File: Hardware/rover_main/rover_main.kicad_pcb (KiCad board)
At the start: 2 copper layers, 85 x 70 mm, 36 parts, among them J1 BATT, J10 Analog, J2 BME280, J3 CSS811, J4 DRIVERS, J5 GY-87, J6 PROG, J7 FTDI, J8 Digital, U1 LD1117A33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

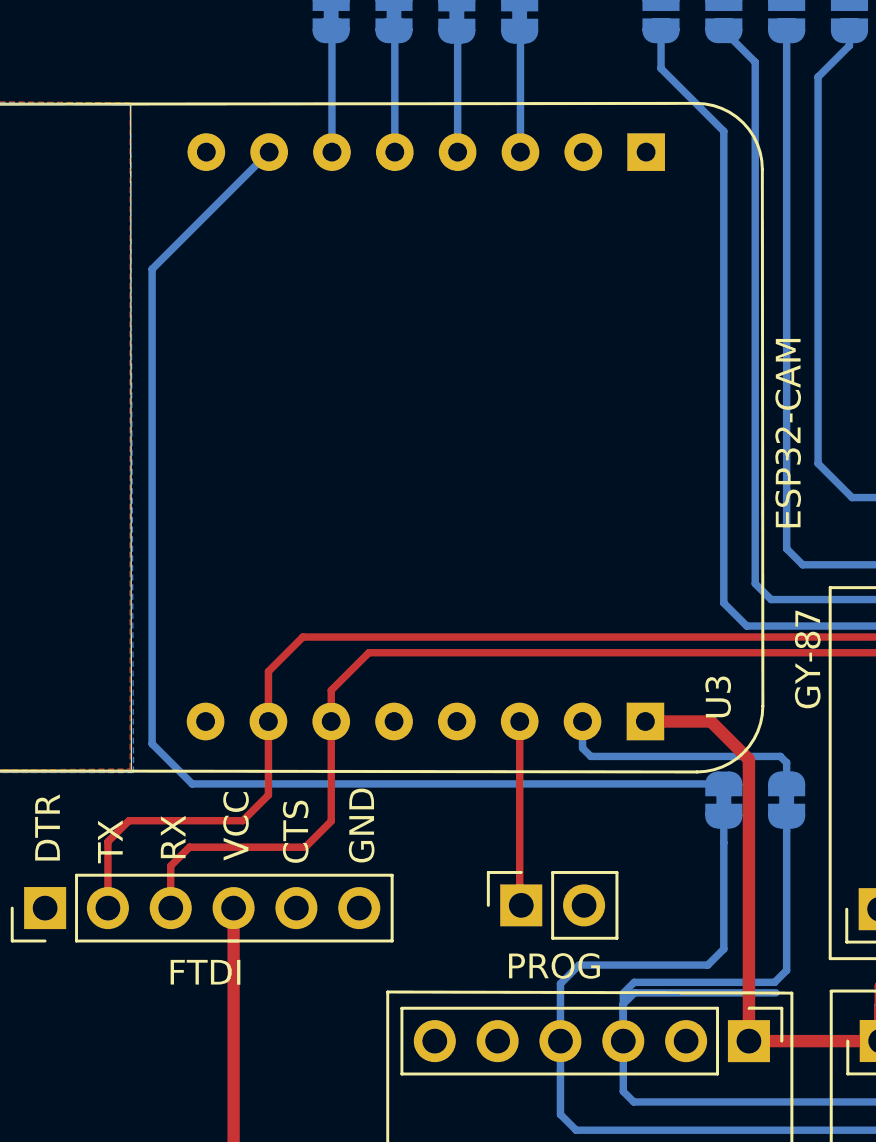
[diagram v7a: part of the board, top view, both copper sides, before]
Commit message: Add SDA to jumper
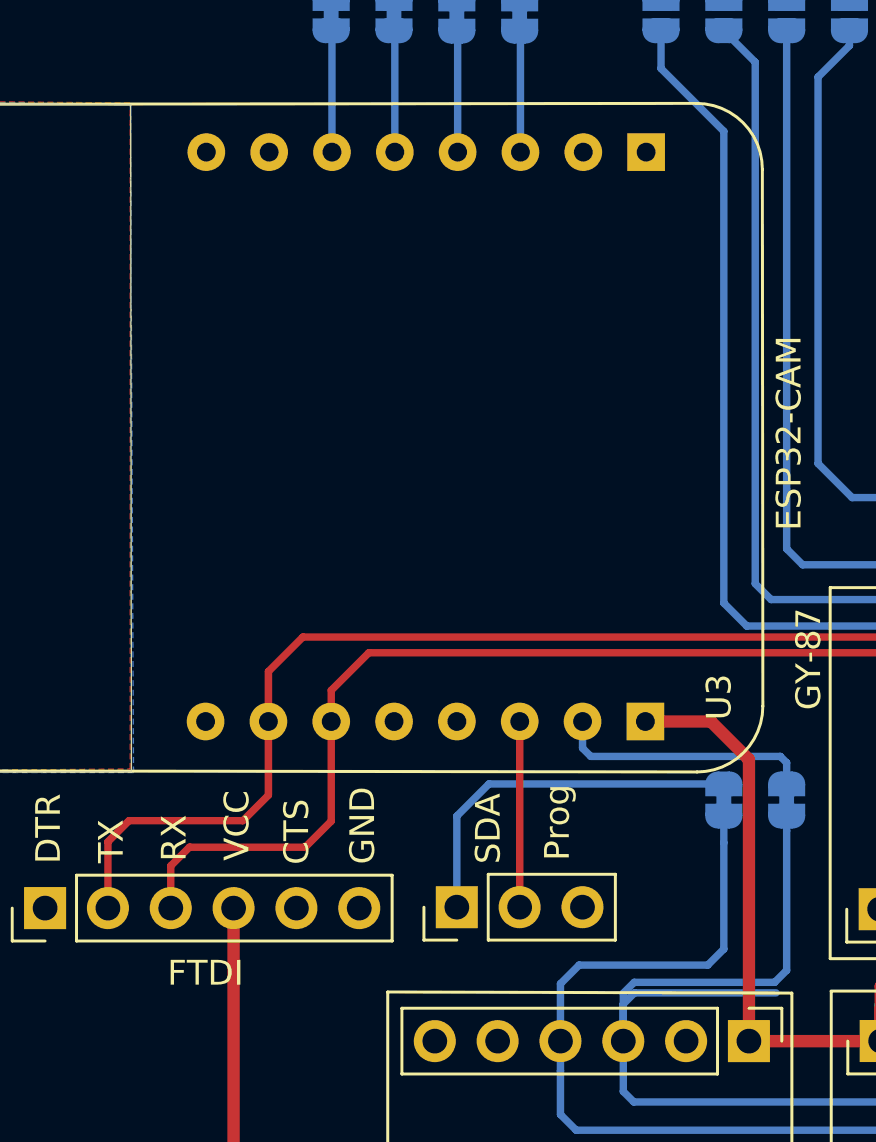
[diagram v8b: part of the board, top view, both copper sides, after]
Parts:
- removed J6: PROG, Connector_PinSocket_2.54mm:PinSocket_1x02_P2.54mm_Vertical
- added SDA: Prog, Connector_PinHeader_2.54mm:PinHeader_1x03_P2.54mm_Vertical, F.Cu at (127.6, 108.8)
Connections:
- U3 pad 15: /SDAE -> /GPIO2
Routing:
- net /SDAE: track 49.7 -> 15.0 mm
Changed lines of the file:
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@@
     (thickness 1.6)
     (drawings 6343)
-    (tracks 308)
+    (tracks 306)
     (zones 0)
     (modules 36)
-    (nets 56)
+    (nets 57)
   )
   (page A4)
@@
   (net 54 "Net-(J2-Pad5)")
   (net 55 "Net-(D3-Pad1)")
+  (net 56 /GPIO2)
   (net_class Default "Esta es la clase de red por defecto."
     (clearance 0.3)
@@
     (add_net /GPIO15)
     (add_net /GPIO15E)
+    (add_net /GPIO2)
     (add_net /GPIO4)
     (add_net /INTA)
@@
     (add_net VCC)
   )
+  (module Connector_PinHeader_2.54mm:PinHeader_1x03_P2.54mm_Vertical (layer F.Cu)
+    (at 127.635 108.839 90)
+    (descr "Through hole straight pin header, 1x03, 2.54mm pitch, single row")
+    (tags "Through hole pin header THT 1x03 2.54mm single row")
+    (fp_text reference SDA (at 3.175 1.27 90) (layer F.SilkS)
+      (effects (font (size 1 1) (thickness 0.15)))
+    )
+    (fp_text value Prog (at 3.429 4.064 90) (layer F.SilkS)
+      (effects (font (size 1 1) (thickness 0.15)))
+    )
+    (fp_text user %R (at 0 2.54 180) (layer F.Fab)
+      (effects (font (size 1 1) (thickness 0.15)))
+    )
+    (fp_line (start 1.8 -1.8) (end -1.8 -1.8) (layer F.CrtYd) (width 0.05))
+    (fp_line (start 1.8 6.85) (end 1.8 -1.8) (layer F.CrtYd) (width 0.05))
+    (fp_line (start -1.8 6.85) (end 1.8 6.85) (layer F.CrtYd) (width 0.05))
+    (fp_line (start -1.8 -1.8) (end -1.8 6.85) (layer F.CrtYd) (width 0.05))
+    (fp_line (start -1.33 -1.33) (end 0 -1.33) (layer F.SilkS) (width 0.12))
+    (fp_line (start -1.33 0) (end -1.33 -1.33) (layer F.SilkS) (width 0.12))
+    (fp_line (start -1.33 1.27) (end 1.33 1.27) (layer F.SilkS) (width 0.12))
+    (fp_line (start 1.33 1.27) (end 1.33 6.41) (layer F.SilkS) (width 0.12))
+    (fp_line (start -1.33 1.27) (end -1.33 6.41) (layer F.SilkS) (width 0.12))
+    (fp_line (start -1.33 6.41) (end 1.33 6.41) (layer F.SilkS) (width 0.12))
+    (fp_line (start -1.27 -0.635) (end -0.635 -1.27) (layer F.Fab) (width 0.1))
+    (fp_line (start -1.27 6.35) (end -1.27 -0.635) (layer F.Fab) (width 0.1))
+    (fp_line (start 1.27 6.35) (end -1.27 6.35) (layer F.Fab) (width 0.1))
+    (fp_line (start 1.27 -1.27) (end 1.27 6.35) (layer F.Fab) (width 0.1))
+    (fp_line (start -0.635 -1.27) (end 1.27 -1.27) (layer F.Fab) (width 0.1))
+    (pad 3 thru_hole oval (at 0 5.08 90) (size 1.7 1.7) (drill 1) (layers *.Cu *.Mask)
+      (net 1 GND))
+    (pad 2 thru_hole oval (at 0 2.54 90) (size 1.7 1.7) (drill 1) (layers *.Cu *.Mask)
+      (net 20 /GPIO0))
+    (pad 1 thru_hole rect (at 0 0 90) (size 1.7 1.7) (drill 1) (layers *.Cu *.Mask)
+      (net 51 /SDAE))
+    (model ${KISYS3DMOD}/Connector_PinHeader_2.54mm.3dshapes/PinHeader_1x03_P2.54mm_Vertical.wrl
+      (at (xyz 0 0 0))
+      (scale (xyz 1 1 1))
+      (rotate (xyz 0 0 0))
+    )
+  )
   (module Diode_THT:D_A-405_P10.16mm_Horizontal (layer F.Cu)
     (at 166.7764 68.4784 270)
@@
     )
   )
-  (module Connector_PinSocket_2.54mm:PinSocket_1x02_P2.54mm_Vertical (layer F.Cu)
-    (at 130.24 108.766 90)
-    (descr "Through hole straight socket strip, 1x02, 2.54mm pitch, single row (from Kicad 4.0.7), script generated")
-    (tags "Through hole socket strip THT 1x02 2.54mm single row")
-    (fp_text reference J6 (at 0 5.27 90) (layer F.CrtYd)
-      (effects (font (size 1 1) (thickness 0.15)))
-    )
-    (fp_text value PROG (at -2.486 1.332 180) (layer F.SilkS)
-      (effects (font (size 1 1) (thickness 0.15)))
-    )
-    (fp_text user %R (at 0 1.27 -180) (layer F.Fab)
-      (effects (font (size 1 1) (thickness 0.15)))
-    )
-    (fp_line (start -1.8 4.3) (end -1.8 -1.8) (layer F.CrtYd) (width 0.05))
-    (fp_line (start 1.75 4.3) (end -1.8 4.3) (layer F.CrtYd) (width 0.05))
-    (fp_line (start 1.75 -1.8) (end 1.75 4.3) (layer F.CrtYd) (width 0.05))
-    (fp_line (start -1.8 -1.8) (end 1.75 -1.8) (layer F.CrtYd) (width 0.05))
-    (fp_line (start 0 -1.33) (end 1.33 -1.33) (layer F.SilkS) (width 0.12))
-    (fp_line (start 1.33 -1.33) (end 1.33 0) (layer F.SilkS) (width 0.12))
-    (fp_line (start 1.33 1.27) (end 1.33 3.87) (layer F.SilkS) (width 0.12))
-    (fp_line (start -1.33 3.87) (end 1.33 3.87) (layer F.SilkS) (width 0.12))
-    (fp_line (start -1.33 1.27) (end -1.33 3.87) (layer F.SilkS) (width 0.12))
-    (fp_line (start -1.33 1.27) (end 1.33 1.27) (layer F.SilkS) (width 0.12))
-    (fp_line (start -1.27 3.81) (end -1.27 -1.27) (layer F.Fab) (width 0.1))
-    (fp_line (start 1.27 3.81) (end -1.27 3.81) (layer F.Fab) (width 0.1))
-    (fp_line (start 1.27 -0.635) (end 1.27 3.81) (layer F.Fab) (width 0.1))
-    (fp_line (start 0.635 -1.27) (end 1.27 -0.635) (layer F.Fab) (width 0.1))
-    (fp_line (start -1.27 -1.27) (end 0.635 -1.27) (layer F.Fab) (width 0.1))
-    (pad 2 thru_hole oval (at 0 2.54 90) (size 1.7 1.7) (drill 1) (layers *.Cu *.Mask)
-      (net 1 GND))
-    (pad 1 thru_hole rect (at 0 0 90) (size 1.7 1.7) (drill 1) (layers *.Cu *.Mask)
-      (net 20 /GPIO0))
-    (model ${KISYS3DMOD}/Connector_PinSocket_2.54mm.3dshapes/PinSocket_1x02_P2.54mm_Vertical.wrl
-      (at (xyz 0 0 0))
-      (scale (xyz 1 1 1))
-      (rotate (xyz 0 0 0))
-    )
-  )
   (module Jumper:SolderJumper-2_P1.3mm_Open_RoundedPad1.0x1.5mm (layer B.Cu)
     (at 143.51 72.756 90)
@@
       (net 13 /GPIO4))
     (pad 15 thru_hole circle (at 11.53 -4.69 90) (size 1.524 1.524) (drill 0.762) (layers *.Cu *.Mask)
-      (net 51 /SDAE))
+      (net 56 /GPIO2))
     (pad 14 thru_hole circle (at 11.53 -2.15 90) (size 1.524 1.524) (drill 0.762) (layers *.Cu *.Mask)
       (net 47 /GPIO14E))
@@
   (segment (start 149.636 67.74) (end 149.636 97.084) (width 0.3) (layer F.Cu) (net 18))
   (segment (start 121.412 97.917) (end 148.803 97.917) (width 0.3) (layer F.Cu) (net 18))
-  (segment (start 130.44 108.726) (end 130.41 108.756) (width 0.3) (layer F.Cu) (net 20))
   (segment (start 130.178 108.704) (end 130.24 108.766) (width 0.3) (layer F.Cu) (net 20))
   (segment (start 130.178 101.332) (end 130.178 108.704) (width 0.3) (layer F.Cu) (net 20))
@@
   (segment (start 127.668 73.454) (end 127.635 73.421) (width 0.3) (layer B.Cu) (net 50))
   (segment (start 127.668 78.312) (end 127.668 73.454) (width 0.3) (layer B.Cu) (net 50))
-  (segment (start 115.316 83.044) (end 120.048 78.312) (width 0.3) (layer B.Cu) (net 51))
-  (segment (start 115.316 102.235) (end 115.316 83.044) (width 0.3) (layer B.Cu) (net 51))
-  (segment (start 138.43 103.856) (end 116.937 103.856) (width 0.3) (layer B.Cu) (net 51))
-  (segment (start 116.937 103.856) (end 115.316 102.235) (width 0.3) (layer B.Cu) (net 51))
+  (segment (start 127.635 105.156) (end 127.635 108.839) (width 0.3) (layer B.Cu) (net 51))
+  (segment (start 128.935 103.856) (end 127.635 105.156) (width 0.3) (layer B.Cu) (net 51))
+  (segment (start 138.43 103.856) (end 128.935 103.856) (width 0.3) (layer B.Cu) (net 51))
   (segment (start 132.718 101.332) (end 132.718 102.40963) (width 0.3) (layer B.Cu) (net 52))
   (segment (start 140.97 103.856) (end 140.97 102.997) (width 0.3) (layer B.Cu) (net 52))
